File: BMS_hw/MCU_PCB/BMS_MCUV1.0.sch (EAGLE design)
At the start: 36 parts, among them IC2 SST25VF020B804ISA, Q1 CRYSTALS-GND-LID-IQXC-42

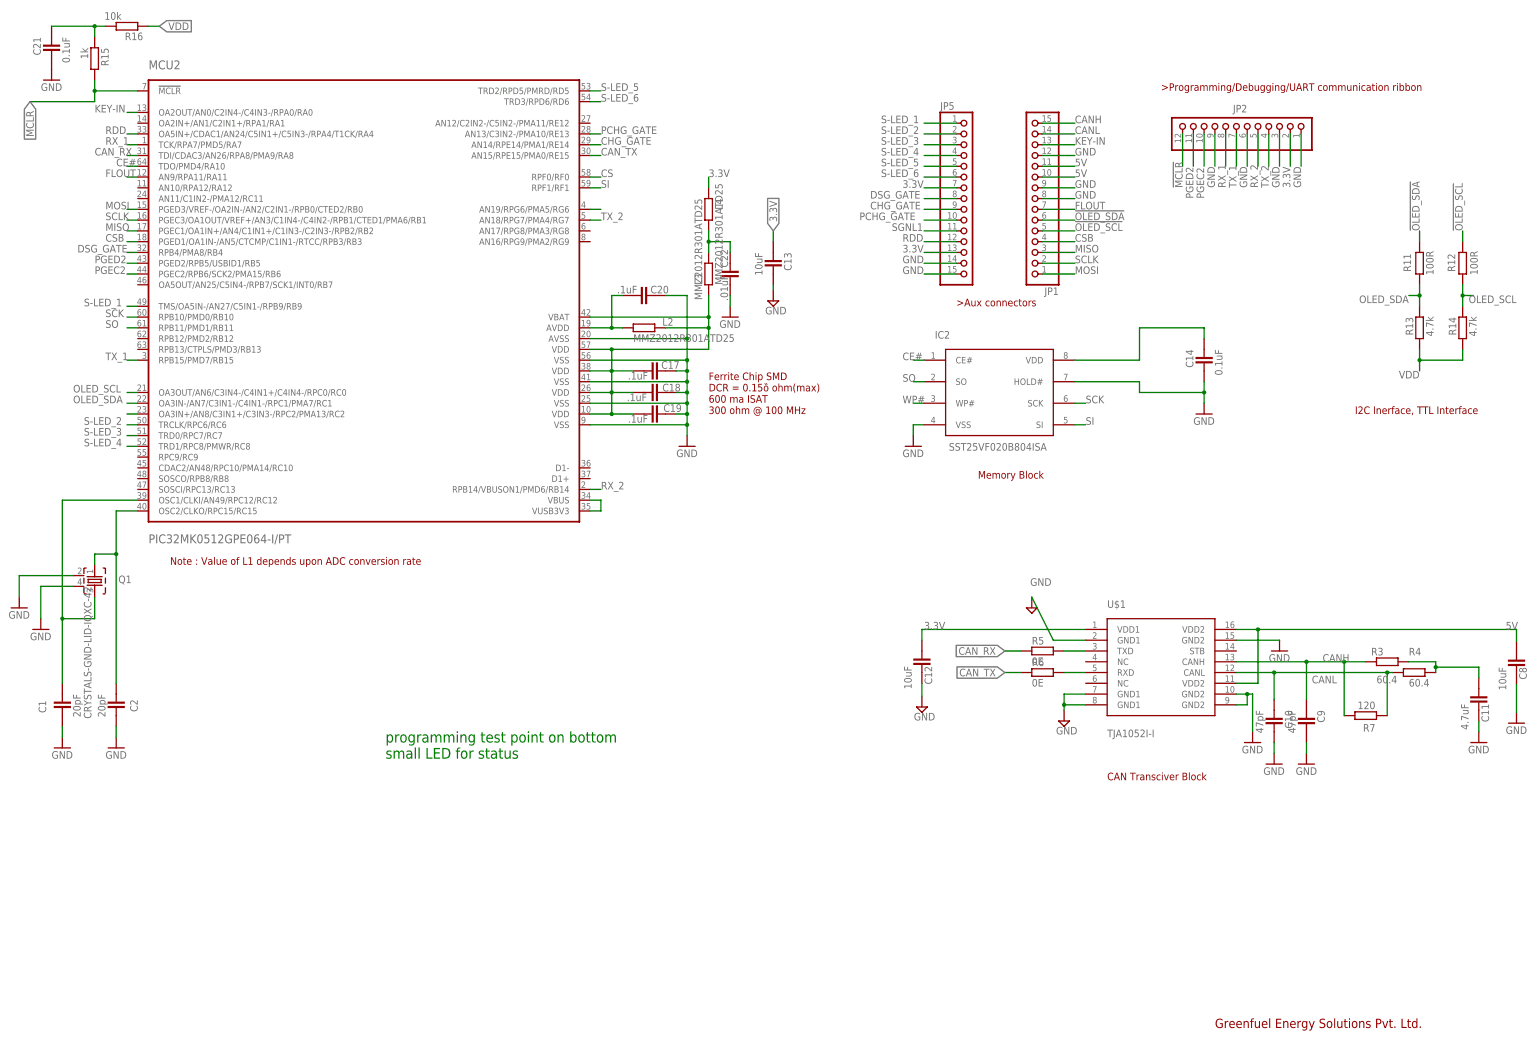
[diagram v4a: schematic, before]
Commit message: afe and piggy board bom layout and schematic all changed for final only dc-dc convertor replacement required !
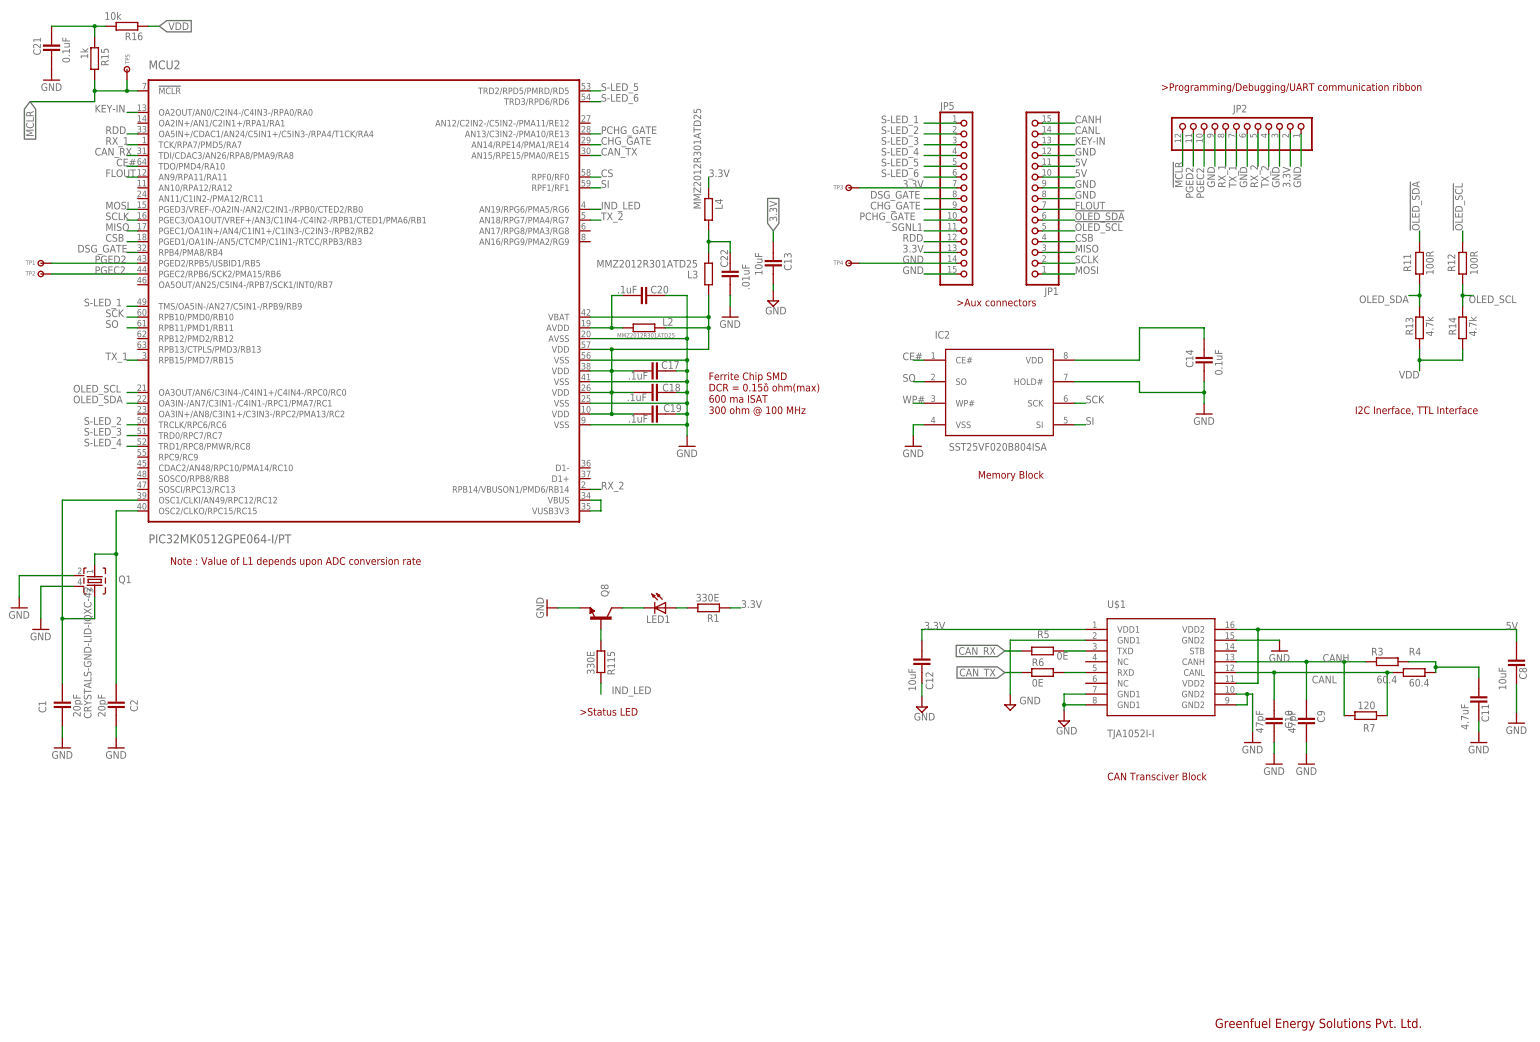
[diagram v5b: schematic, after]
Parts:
- added LED1: (no value), adafruit:LEDCHIP-LED0603
- added Q8: (no value), ipc-7351-transistor:NPN_SOT-23
- added R1, R115: 330E, ipc-7351-resistor:RESISTOR_0402
- added TP1, TP2, TP3, TP4, TP5: TP-SMD60, simpa:TP-SMD60
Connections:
- removed net N$44: MCU2.AN19/RPG6/PMA5/RG6
- removed net N$73: MCU2.OA3IN+/AN8/C3IN1+/C3IN3-/RPC2/PMA13/RC2
- new net IND_LED: MCU2.AN19/RPG6/PMA5/RG6, R115.2
- new net N$5: LED1.A, R1.2
- new net N$8: LED1.C, Q8.C
- net !MCLR: now also TP5.P$1
- net 3.3V: now also R1.1, TP3.P$1
- net GND: now also Q8.E, TP4.P$1, U$1.GND1
- net N$7: now also Q8.B, R115.1; no longer U$1.GND1
- net PGEC2: now also TP2.P$1
- net PGED2: now also TP1.P$1
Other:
- note removed: "programming test point on bottom small LED for status"

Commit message: afe and piggy sch layout itt!
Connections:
- removed net N$4: C14.1, IC2.VDD
- net 3.3V: now also C14.1, IC2.VDD
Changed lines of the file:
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@@
 <label x="177.8" y="111.76" size="1.778" layer="95"/>
+</segment>
+<segment>
+<pinref part="IC2" gate="G$1" pin="VDD"/>
+<wire x1="256.54" y1="170.18" x2="271.78" y2="170.18" width="0.1524" layer="91"/>
+<wire x1="271.78" y1="170.18" x2="271.78" y2="177.8" width="0.1524" layer="91"/>
+<wire x1="271.78" y1="177.8" x2="287.02" y2="177.8" width="0.1524" layer="91"/>
+<pinref part="C14" gate="G$1" pin="1"/>
+<wire x1="287.02" y1="177.8" x2="287.02" y2="175.26" width="0.1524" layer="91"/>
+<label x="276.86" y="177.8" size="1.778" layer="95"/>
 </segment>
 </net>
@@
 </segment>
 </net>
-<net name="N$4" class="0">
-<segment>
-<pinref part="IC2" gate="G$1" pin="VDD"/>
-<wire x1="256.54" y1="170.18" x2="271.78" y2="170.18" width="0.1524" layer="91"/>
-<wire x1="271.78" y1="170.18" x2="271.78" y2="177.8" width="0.1524" layer="91"/>
-<wire x1="271.78" y1="177.8" x2="287.02" y2="177.8" width="0.1524" layer="91"/>
-<pinref part="C14" gate="G$1" pin="1"/>
-<wire x1="287.02" y1="177.8" x2="287.02" y2="175.26" width="0.1524" layer="91"/>
-</segment>
-</net>

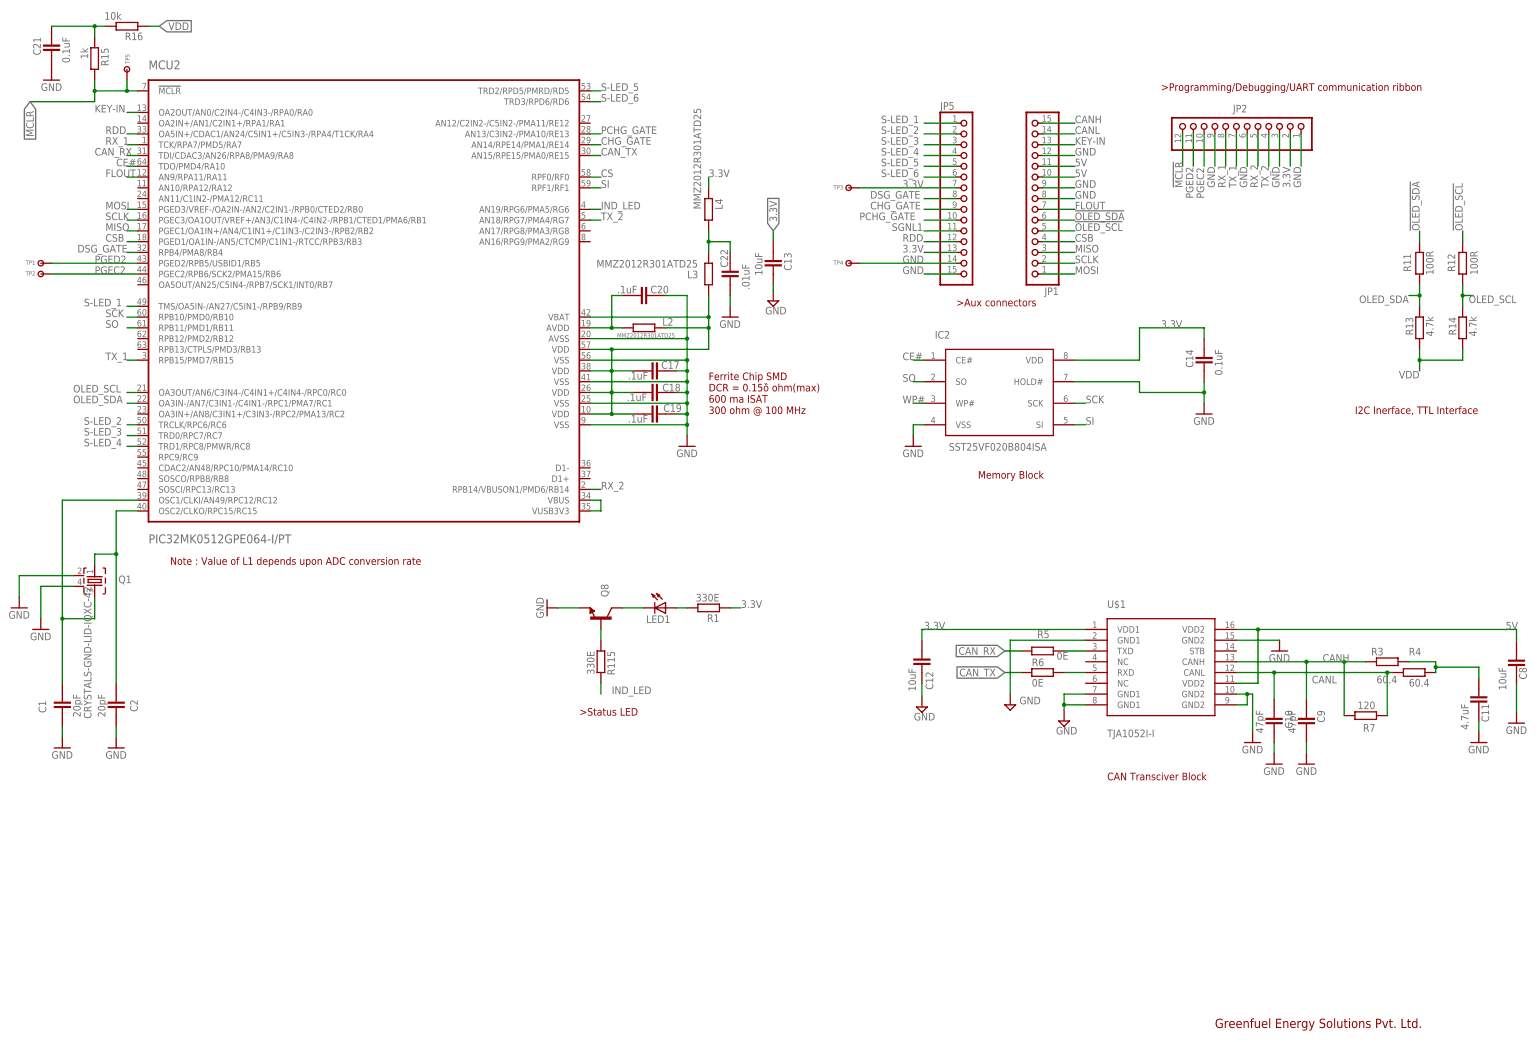
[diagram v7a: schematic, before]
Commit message: updated afe shmetatic rectification stage of MCU PCB
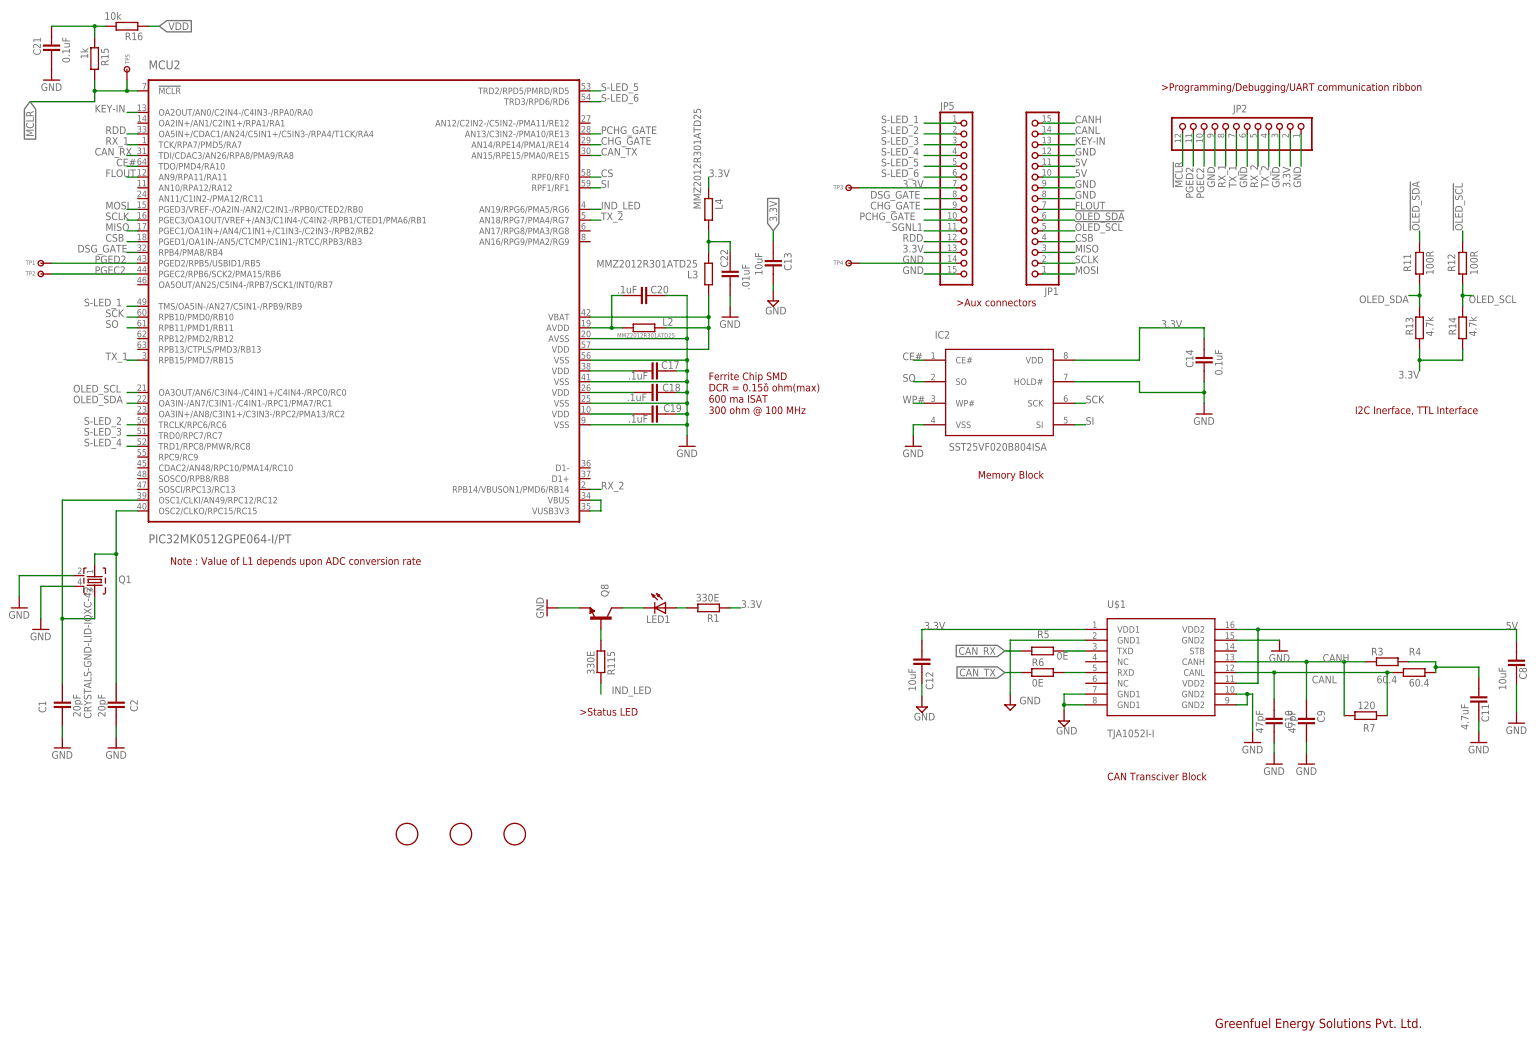
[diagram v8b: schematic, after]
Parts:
- added U$2, U$3, U$4: FIDUCIAL, adafruit:FIDUCIAL
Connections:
- new net N$4: C19.1, MCU2.VDD
- new net N$9: C18.1, MCU2.VDD@1
- new net VDD38: C17.1, MCU2.VDD@2
- net 3.3V: now also R13.1, R14.1
- net VDD: no longer C17.1, C18.1, C19.1, MCU2.VDD, MCU2.VDD@1, MCU2.VDD@2, R13.1, R14.1
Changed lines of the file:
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@@
 <part name="TP4" library="simpa" deviceset="TP" device="-SMD60"/>
 <part name="TP5" library="simpa" deviceset="TP" device="-SMD60"/>
+<part name="U$2" library="adafruit" deviceset="FIDUCIAL" device=""/>
+<part name="U$3" library="adafruit" deviceset="FIDUCIAL" device=""/>
+<part name="U$4" library="adafruit" deviceset="FIDUCIAL" device=""/>
 </parts>
 <sheets>
@@
 <attribute name="NAME" x="33.655" y="240.03" size="1.016" layer="95" font="vector" ratio="12" rot="R90"/>
 </instance>
+<instance part="U$2" gate="G$1" x="99.06" y="58.42" smashed="yes"/>
+<instance part="U$3" gate="G$1" x="111.76" y="58.42" smashed="yes"/>
+<instance part="U$4" gate="G$1" x="124.46" y="58.42" smashed="yes"/>
 </instances>
 <busses>
@@
 <label x="276.86" y="177.8" size="1.778" layer="95"/>
 </segment>
+<segment>
+<pinref part="R14" gate="G$1" pin="1"/>
+<wire x1="337.82" y1="170.18" x2="347.98" y2="170.18" width="0.1524" layer="91"/>
+<wire x1="347.98" y1="170.18" x2="347.98" y2="172.72" width="0.1524" layer="91"/>
+<pinref part="R13" gate="G$1" pin="1"/>
+<wire x1="337.82" y1="172.72" x2="337.82" y2="170.18" width="0.1524" layer="91"/>
+<junction x="337.82" y="170.18"/>
+<wire x1="337.82" y1="170.18" x2="337.82" y2="167.64" width="0.1524" layer="91"/>
+<label x="337.82" y="167.64" size="1.778" layer="95" font="vector" ratio="12" rot="R180"/>
+</segment>
 </net>
 <net name="N$6" class="0">
@@
 <net name="VDD" class="0">
 <segment>
-<pinref part="R14" gate="G$1" pin="1"/>
-<wire x1="337.82" y1="170.18" x2="347.98" y2="170.18" width="0.1524" layer="91"/>
-<wire x1="347.98" y1="170.18" x2="347.98" y2="172.72" width="0.1524" layer="91"/>
-<pinref part="R13" gate="G$1" pin="1"/>
-<wire x1="337.82" y1="172.72" x2="337.82" y2="170.18" width="0.1524" layer="91"/>
-<junction x="337.82" y="170.18"/>
-<wire x1="337.82" y1="170.18" x2="337.82" y2="167.64" width="0.1524" layer="91"/>
-<label x="337.82" y="167.64" size="1.778" layer="95" font="vector" ratio="12" rot="R180"/>
-</segment>
-<segment>
-<pinref part="MCU2" gate="G$1" pin="VDD"/>
-<pinref part="C19" gate="G$1" pin="1"/>
-<wire x1="142.24" y1="157.48" x2="147.32" y2="157.48" width="0.1524" layer="91"/>
-<wire x1="147.32" y1="157.48" x2="152.4" y2="157.48" width="0.1524" layer="91"/>
-<wire x1="147.32" y1="157.48" x2="147.32" y2="162.56" width="0.1524" layer="91"/>
-<wire x1="147.32" y1="162.56" x2="147.32" y2="167.64" width="0.1524" layer="91"/>
-<wire x1="147.32" y1="167.64" x2="147.32" y2="172.72" width="0.1524" layer="91"/>
-<junction x="147.32" y="157.48"/>
-<pinref part="MCU2" gate="G$1" pin="VDD@1"/>
-<pinref part="C18" gate="G$1" pin="1"/>
-<wire x1="142.24" y1="162.56" x2="147.32" y2="162.56" width="0.1524" layer="91"/>
-<junction x="147.32" y="162.56"/>
-<wire x1="147.32" y1="162.56" x2="152.4" y2="162.56" width="0.1524" layer="91"/>
-<pinref part="MCU2" gate="G$1" pin="VDD@2"/>
-<pinref part="C17" gate="G$1" pin="1"/>
-<wire x1="142.24" y1="167.64" x2="147.32" y2="167.64" width="0.1524" layer="91"/>
-<junction x="147.32" y="167.64"/>
-<wire x1="147.32" y1="167.64" x2="152.4" y2="167.64" width="0.1524" layer="91"/>
 <pinref part="L2" gate="G$1" pin="2"/>
 <wire x1="160.02" y1="177.8" x2="170.18" y2="177.8" width="0.1524" layer="91"/>
 <wire x1="170.18" y1="177.8" x2="170.18" y2="172.72" width="0.1524" layer="91"/>
-<wire x1="170.18" y1="172.72" x2="147.32" y2="172.72" width="0.1524" layer="91"/>
+<wire x1="170.18" y1="172.72" x2="142.24" y2="172.72" width="0.1524" layer="91"/>
 <pinref part="MCU2" gate="G$1" pin="VDD@3"/>
-<wire x1="142.24" y1="172.72" x2="147.32" y2="172.72" width="0.1524" layer="91"/>
-<junction x="147.32" y="172.72"/>
 <wire x1="170.18" y1="177.8" x2="170.18" y2="180.34" width="0.1524" layer="91"/>
 <junction x="170.18" y="177.8"/>
@@
 </segment>
 </net>
+<net name="N$4" class="0">
+<segment>
+<pinref part="C19" gate="G$1" pin="1"/>
+<pinref part="MCU2" gate="G$1" pin="VDD"/>
+<wire x1="142.24" y1="157.48" x2="152.4" y2="157.48" width="0.1524" layer="91"/>
+</segment>
+</net>
+<net name="N$9" class="0">
+<segment>
+<pinref part="C18" gate="G$1" pin="1"/>
+<pinref part="MCU2" gate="G$1" pin="VDD@1"/>
+<wire x1="142.24" y1="162.56" x2="152.4" y2="162.56" width="0.1524" layer="91"/>
+</segment>
+</net>
+<net name="VDD38" class="0">
+<segment>
+<pinref part="C17" gate="G$1" pin="1"/>
+<pinref part="MCU2" gate="G$1" pin="VDD@2"/>
+<wire x1="142.24" y1="167.64" x2="152.4" y2="167.64" width="0.1524" layer="91"/>
+</segment>
+</net>
